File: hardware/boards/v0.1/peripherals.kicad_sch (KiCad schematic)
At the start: 9 parts, among them IC2 DA7280-00FVC, M1 LRA, U21 LSM6DS3

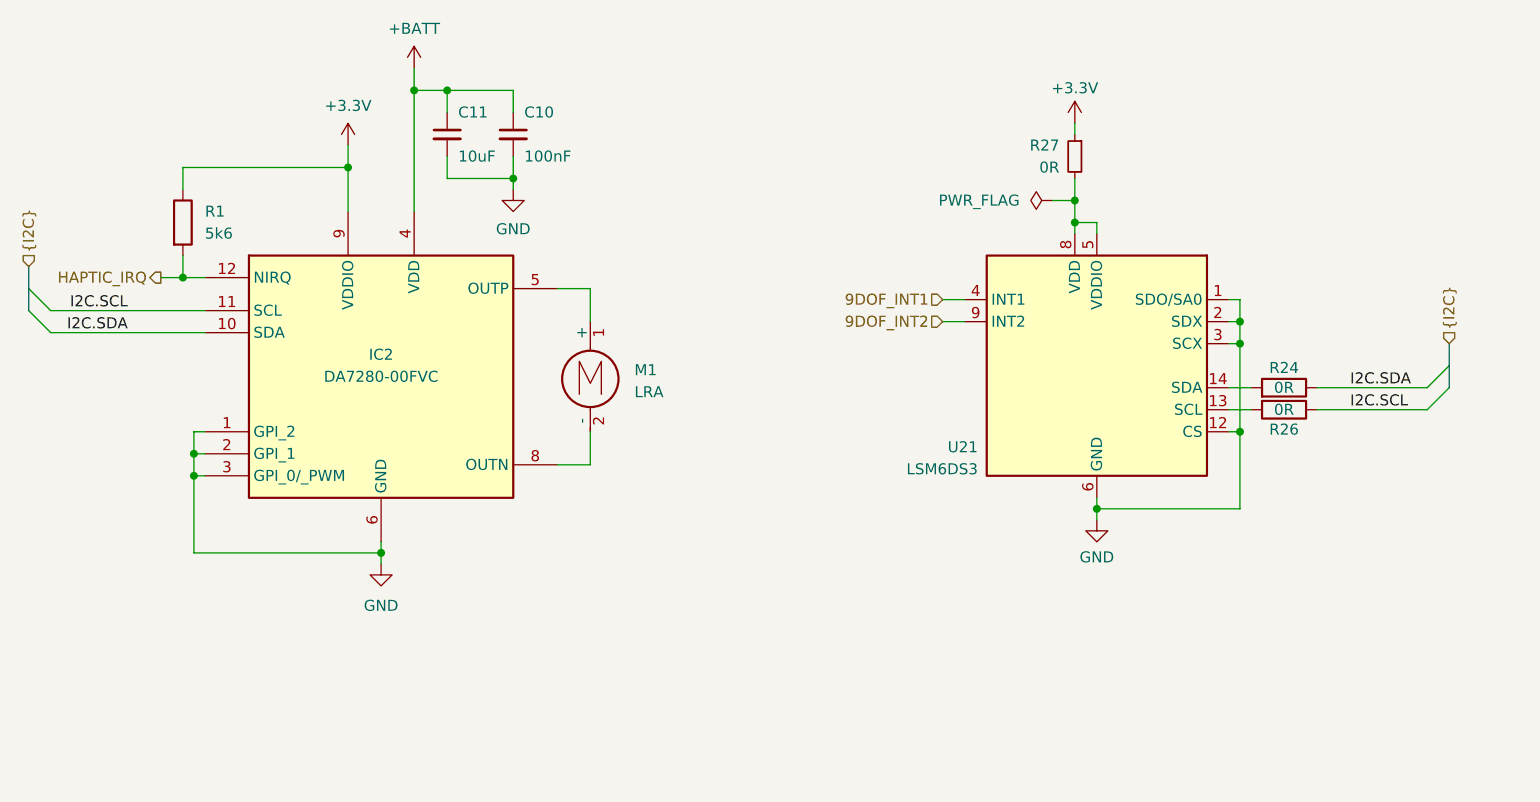
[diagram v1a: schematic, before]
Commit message: feat: route audio components
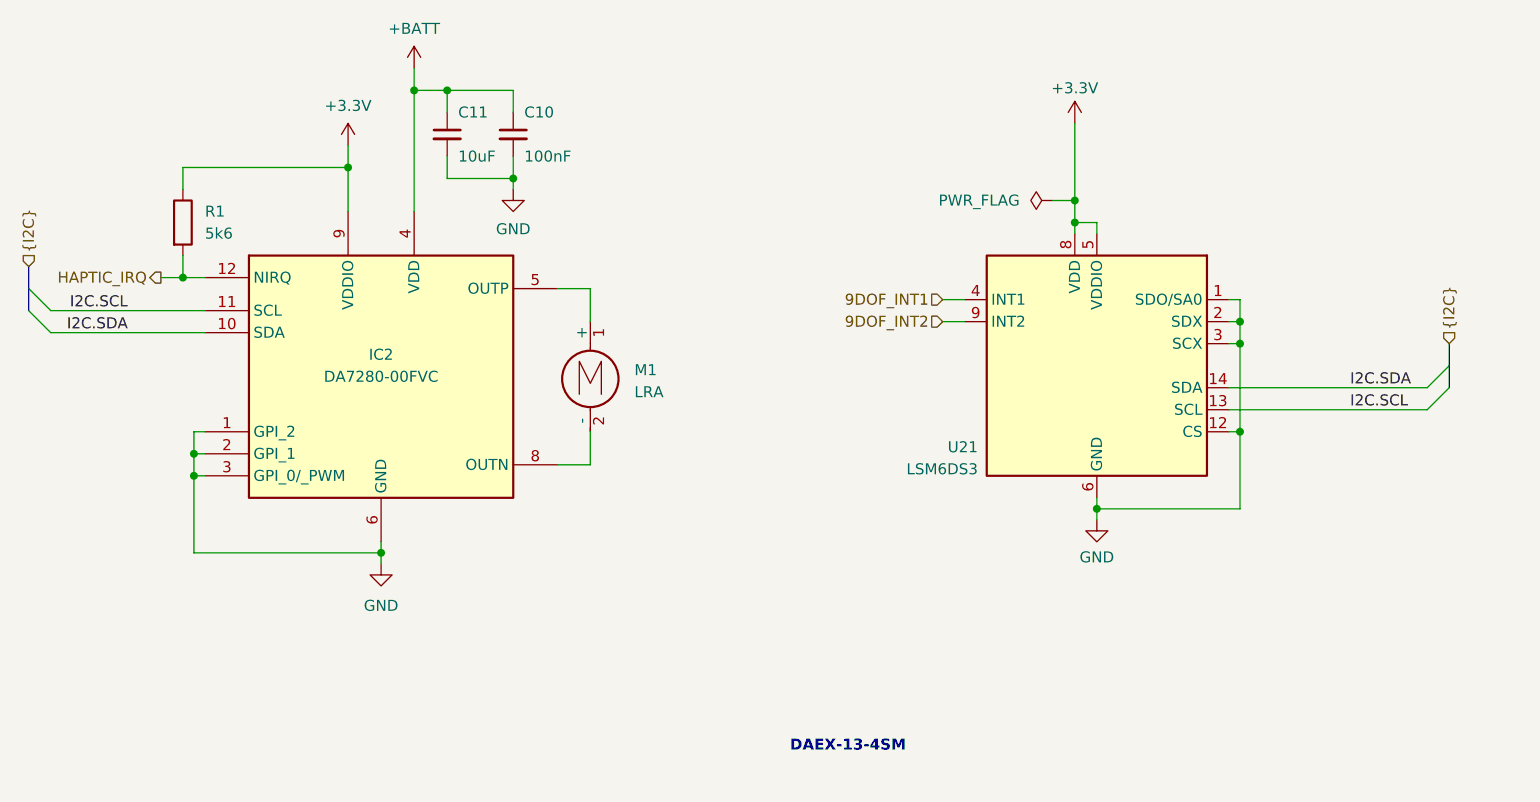
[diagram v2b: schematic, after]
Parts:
- removed R24, R26: 0R, Resistor_SMD:R_0402_1005Metric, symbol Device:R
- removed R27: 0R, Resistor_SMD:R_0402_1005Metric, symbol Device:R_Small
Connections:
- net +3.3V: now also U21.5 (VDDIO), U21.8 (VDD)
- net I2C.SCL: now also U21.13 (SCL)
- net I2C.SDA: now also U21.14 (SDA)
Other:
- note added: "DAEX-13-4SM"

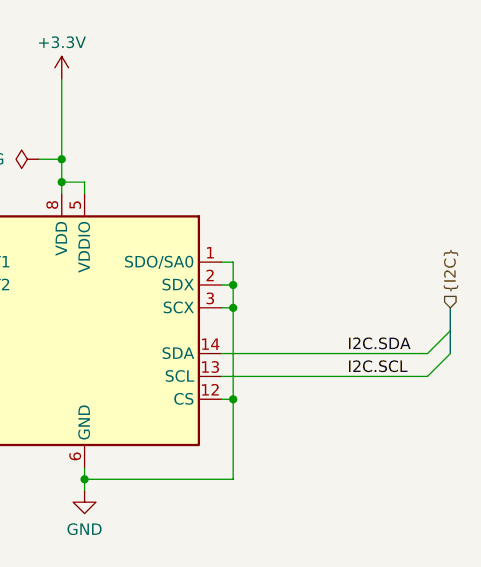
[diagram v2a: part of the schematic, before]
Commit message: feat: route dedicated audio I2C bus
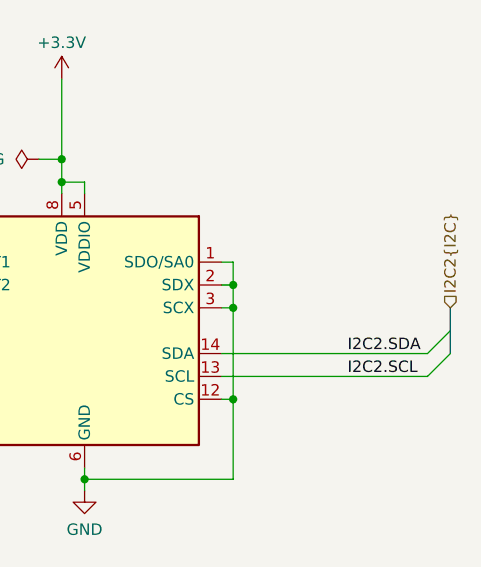
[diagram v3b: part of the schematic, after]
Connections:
- net I2C.SCL: no longer U21.13 (SCL)
- net I2C.SDA: no longer U21.14 (SDA)
- new net I2C2.SCL: U21.13 (SCL)
- new net I2C2.SDA: U21.14 (SDA)
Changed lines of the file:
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@@
 		)
 	)
-	(label "I2C.SDA"
+	(label "I2C2.SDA"
 		(at 173.99 62.23 0)
 		(effects
@@
 		)
 	)
-	(label "I2C.SCL"
+	(label "I2C2.SCL"
 		(at 173.99 64.77 0)
 		(effects
@@
 		)
 	)
-	(hierarchical_label "{I2C}"
+	(hierarchical_label "I2C2{I2C}"
 		(shape input)
 		(at 185.42 57.15 90)

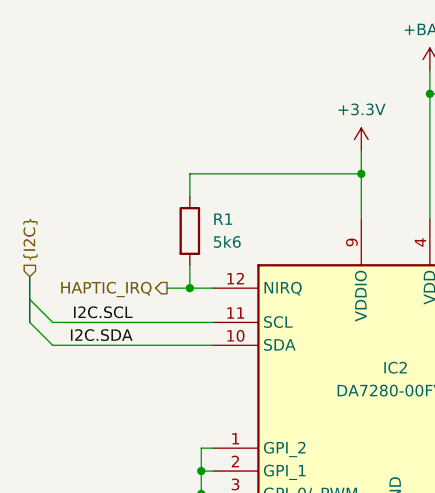
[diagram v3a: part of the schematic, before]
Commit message: feat: schematic organization and ERC cleanup
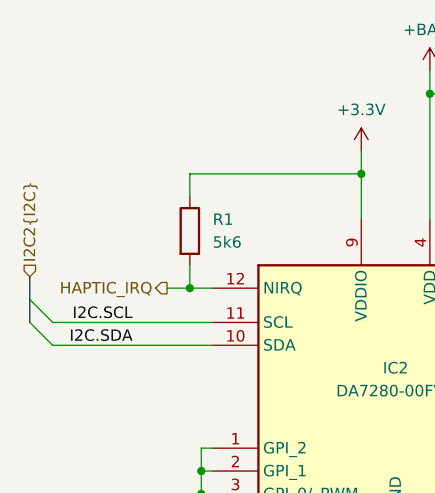
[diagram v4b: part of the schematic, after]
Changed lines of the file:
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@@
 		)
 	)
-	(hierarchical_label "{I2C}"
+	(hierarchical_label "I2C2{I2C}"
 		(shape input)
 		(at 21.59 48.26 90)

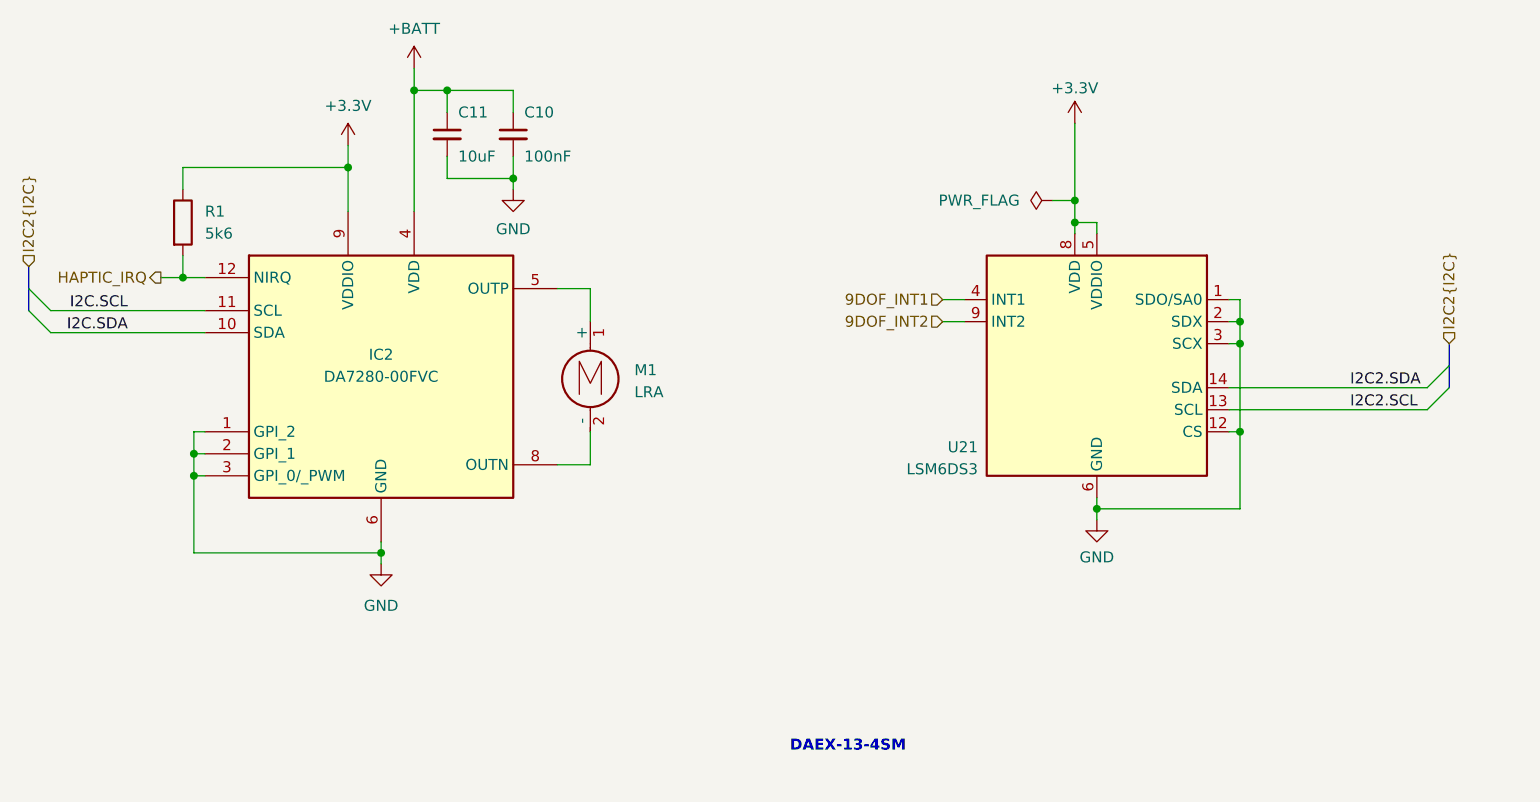
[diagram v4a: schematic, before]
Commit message: feat: various ERC and DRC cleanup
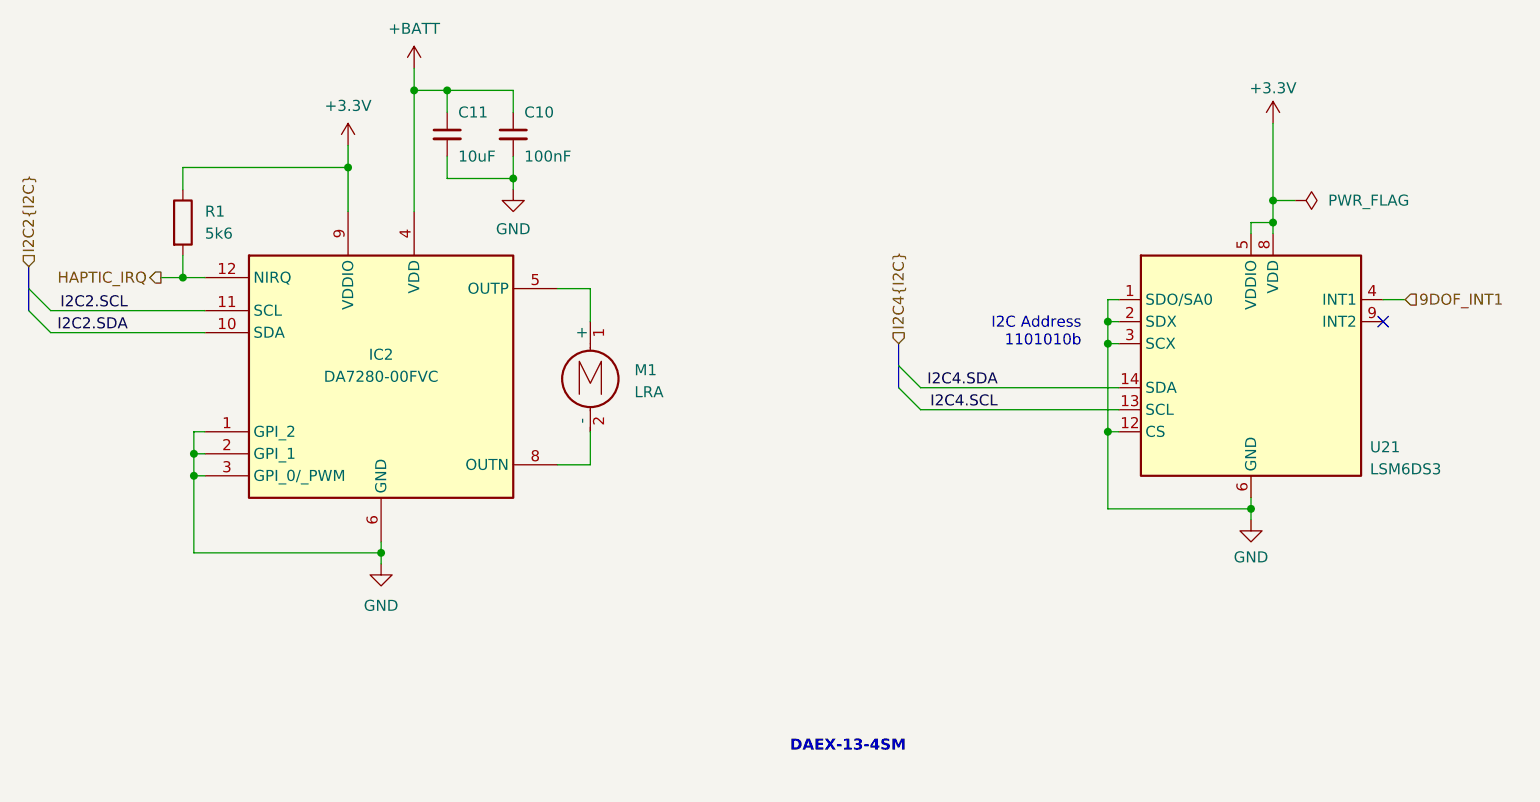
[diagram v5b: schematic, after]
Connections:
- net I2C.SCL is gone; now on net I2C2.SCL: IC2.11 (SCL)
- net I2C.SDA is gone; now on net I2C2.SDA: IC2.10 (SDA)
- net I2C2.SCL: no longer U21.13 (SCL)
- net I2C2.SDA: no longer U21.14 (SDA)
- net 9DOF_INT2: no longer names the net of U21.9 (INT2)
- new net I2C4.SCL: U21.13 (SCL)
- new net I2C4.SDA: U21.14 (SDA)
- no-connect marks 0 -> 1
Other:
- note added: "I2C Address 1101010b"
- moved on the sheet: U21

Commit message: feat: more routing and DRC cleanup
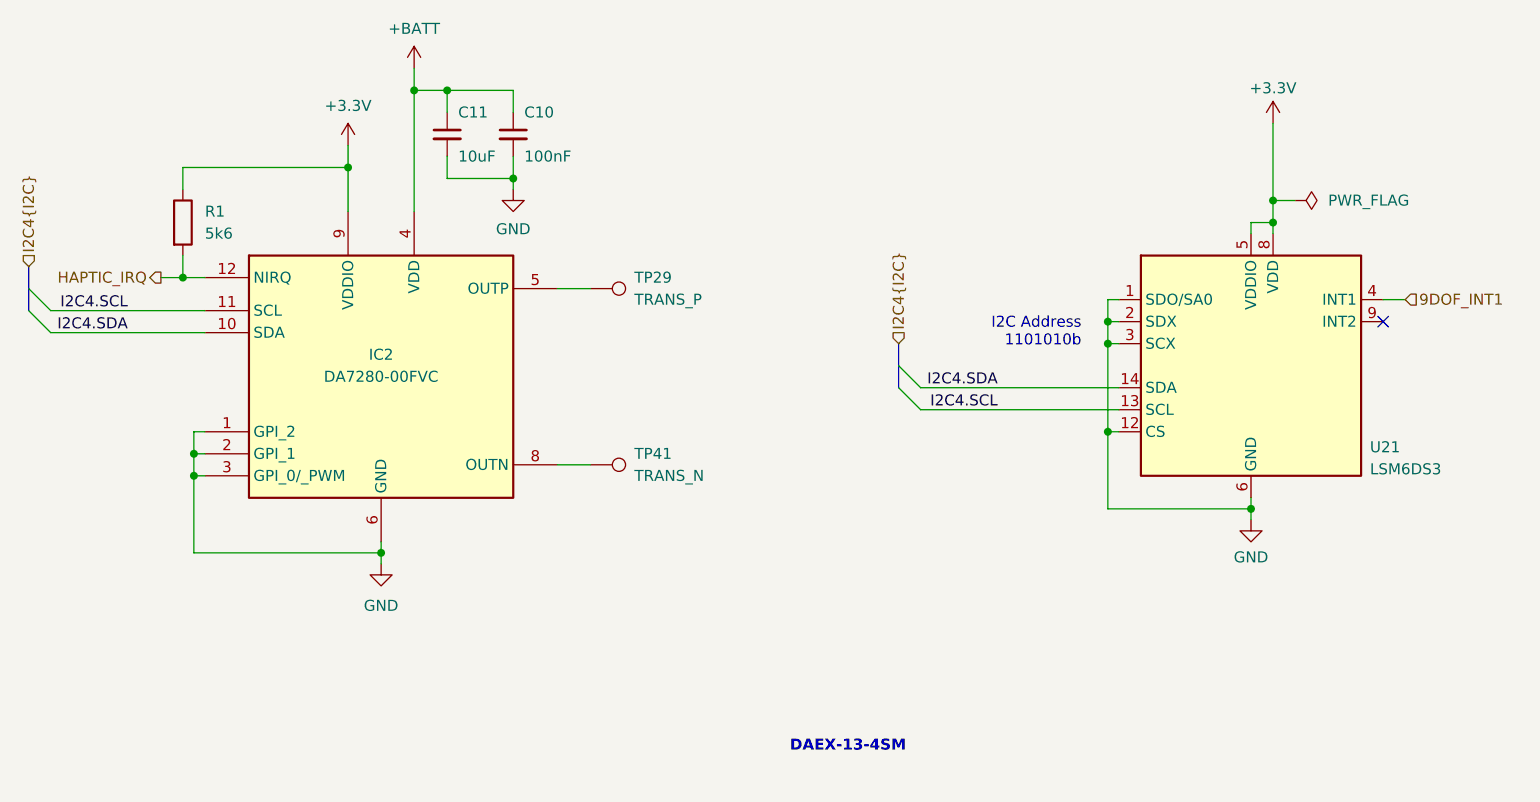
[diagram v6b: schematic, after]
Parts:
- removed M1: LRA, symbol Motor:Motor_DC
- added TP29: TRANS_P, TestPoint:TestPoint_Pad_D2.5mm, symbol Connector:TestPoint
- added TP41: TRANS_N, TestPoint:TestPoint_Pad_D2.5mm, symbol Connector:TestPoint
- R1: footprint (none) -> Resistor_SMD:R_0603_1608Metric
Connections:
- net I2C2.SCL is gone; now on net I2C4.SCL: IC2.11 (SCL)
- net I2C2.SDA is gone; now on net I2C4.SDA: IC2.10 (SDA)
- net at IC2.5 (OUTP): now also TP29.1
- net at IC2.8 (OUTN): now also TP41.1
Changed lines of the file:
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@@
-	(wire
-		(pts
-			(xy 86.36 50.8) (xy 86.36 54.61)
-		)
-		(stroke
-			(width 0)
-			(type default)
-		)
-	)
 	(wire
 		(pts
@@
 	(wire
 		(pts
-			(xy 86.36 71.12) (xy 86.36 67.31)
-		)
-		(stroke
-			(width 0)
-			(type default)
-		)
-	)
-	(wire
-		(pts
 			(xy 66.04 27.94) (xy 69.85 27.94)
 		)
@@
 		)
 	)
-	(label "I2C2.SCL"
+	(label "I2C4.SCL"
 		(at 33.02 53.34 180)
 		(effects
@@
 		)
 	)
-	(label "I2C2.SDA"
+	(label "I2C4.SDA"
 		(at 33.02 55.88 180)
 		(effects
@@
 		)
 	)
-	(hierarchical_label "I2C2{I2C}"
+	(hierarchical_label "I2C4{I2C}"
 		(shape input)
 		(at 21.59 48.26 90)
@@
 			)
 		)
-		(property "Footprint" ""
+		(property "Footprint" "Resistor_SMD:R_0603_1608Metric"
 			(at 37.592 43.18 90)
 			(effects
@@
 				(path "/485383b8-00f4-4405-b270-de249939cff4/f91e71c7-727a-4ef4-a387-8ca9d7b49c20"
 					(reference "#PWR013")
+					(unit 1)
+				)
+			)
+		)
+	)
+	(symbol
+		(lib_id "Connector:TestPoint")
+		(at 86.36 71.12 270)
+		(unit 1)
+		(exclude_from_sim no)
+		(in_bom yes)
+		(on_board yes)
+		(dnp no)
+		(fields_autoplaced yes)
+		(property "Reference" "TP41"
+			(at 91.44 69.8499 90)
+			(effects
+				(font
+					(size 1.27 1.27)
+				)
+				(justify left)
+			)
+		)
+		(property "Value" "TRANS_N"
+			(at 91.44 72.3899 90)
+			(effects
+				(font
+					(size 1.27 1.27)
+				)
+				(justify left)
+			)
+		)
+		(property "Footprint" "TestPoint:TestPoint_Pad_D2.5mm"
+			(at 86.36 76.2 0)
+			(effects
+				(font
+					(size 1.27 1.27)
+				)
+				(hide yes)
+			)
+		)
+		(property "Datasheet" "~"
+			(at 86.36 76.2 0)
+			(effects
+				(font
+					(size 1.27 1.27)
+				)
+				(hide yes)
+			)
+		)
+		(property "Description" "test point"
+			(at 86.36 71.12 0)
+			(effects
+				(font
+					(size 1.27 1.27)
+				)
+				(hide yes)
+			)
+		)
+		(pin "1"
+		)
+		(instances
+			(project "pocket_synth"
+				(path "/485383b8-00f4-4405-b270-de249939cff4/f91e71c7-727a-4ef4-a387-8ca9d7b49c20"
+					(reference "TP41")
 					(unit 1)
 				)
@@
 	)
 	(symbol
+		(lib_id "Connector:TestPoint")
+		(at 86.36 50.8 270)
+		(unit 1)
+		(exclude_from_sim no)
+		(in_bom yes)
+		(on_board yes)
+		(dnp no)
+		(fields_autoplaced yes)
+		(property "Reference" "TP29"
+			(at 91.44 49.5299 90)
+			(effects
+				(font
+					(size 1.27 1.27)
+				)
+				(justify left)
+			)
+		)
+		(property "Value" "TRANS_P"
+			(at 91.44 52.0699 90)
+			(effects
+				(font
+					(size 1.27 1.27)
+				)
+				(justify left)
+			)
+		)
+		(property "Footprint" "TestPoint:TestPoint_Pad_D2.5mm"
+			(at 86.36 55.88 0)
+			(effects
+				(font
+					(size 1.27 1.27)
+				)
+				(hide yes)
+			)
+		)
+		(property "Datasheet" "~"
+			(at 86.36 55.88 0)
+			(effects
+				(font
+					(size 1.27 1.27)
+				)
+				(hide yes)
+			)
+		)
+		(property "Description" "test point"
+			(at 86.36 50.8 0)
+			(effects
+				(font
+					(size 1.27 1.27)
+				)
+				(hide yes)
+			)
+		)
+		(pin "1"
+		)
+		(instances
+			(project ""
+				(path "/485383b8-00f4-4405-b270-de249939cff4/f91e71c7-727a-4ef4-a387-8ca9d7b49c20"
+					(reference "TP29")
+					(unit 1)
+				)
+			)
+		)
+	)
+	(symbol
 		(lib_id "power:GND")
 		(at 162.56 77.47 0)
@@
 					(unit 1)
 				)
-			)
-		)
-	)
-	(symbol
-		(lib_id "Motor:Motor_DC")
-		(at 86.36 59.69 0)
-		(unit 1)
-		(exclude_from_sim no)
-		(in_bom yes)
-		(on_board yes)
-		(dnp no)
-		(property "Reference" "M1"
-			(at 91.44 60.198 0)
-			(effects
-				(font
-					(size 1.27 1.27)
-				)
-				(justify left)
-			)
-		)
-		(property "Value" "LRA"
-			(at 91.44 62.738 0)
-			(effects
-				(font
-					(size 1.27 1.27)
-				)
-				(justify left)
-			)
-		)
-		(property "Footprint" ""
-			(at 86.36 61.976 0)
-			(effects
-				(font
-					(size 1.27 1.27)
-				)
-				(hide yes)
-			)
-		)
-		(property "Datasheet" "~"
-			(at 86.36 61.976 0)
-			(effects
-				(font
-					(size 1.27 1.27)
-				)
-				(hide yes)
-			)
-		)
-		(property "Description" "DC Motor"
-			(at 86.36 59.69 0)
-			(effects
-				(font
-					(size 1.27 1.27)
-				)
-				(hide yes)
-			)
-		)
-		(property "Connector" ""
-			(at 86.36 59.69 0)
-			(effects
-				(font
-					(size 1.27 1.27)
-				)
-			)
-		)
-		(pin "2"
-		)
-		(pin "1"
-		)
-		(instances
-			(project "pocket_synth"
-				(path "/485383b8-00f4-4405-b270-de249939cff4/f91e71c7-727a-4ef4-a387-8ca9d7b49c20"
-					(reference "M1")
-					(unit 1)
-				)
